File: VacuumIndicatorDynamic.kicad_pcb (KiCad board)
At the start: 2 copper layers, 151.2 x 100 mm, 113 parts, among them J1 Conn_01x02_Male, J2 Conn_01x03_Male, J3 Conn_01x03_Male, J4 Conn_01x03_Male, SW1 SW_DIP_x01, SW2 SW_DIP_x01, SW3 SW_DIP_x01, SW4 SW_DIP_x01, U1 AP1117-25, U2 YAAJ_BluePill

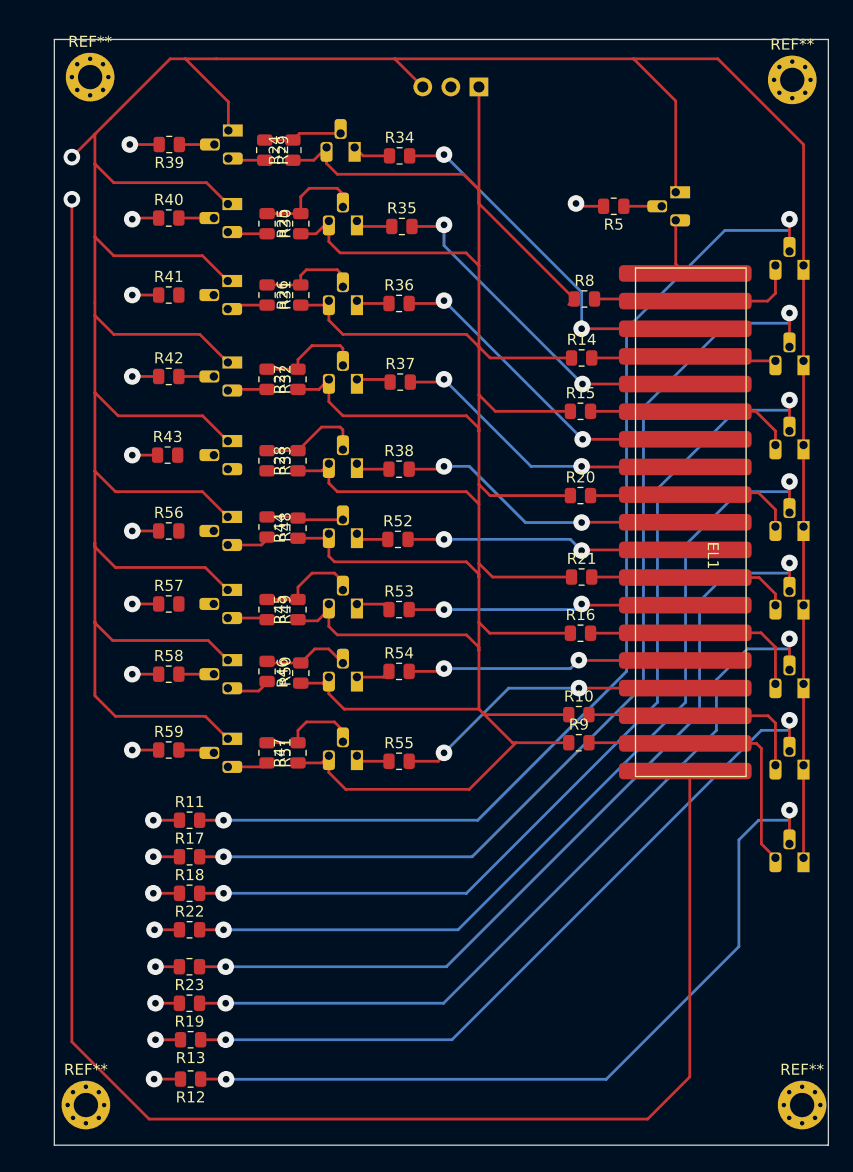
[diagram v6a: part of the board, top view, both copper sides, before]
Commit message: pcb route width update. add small copper area
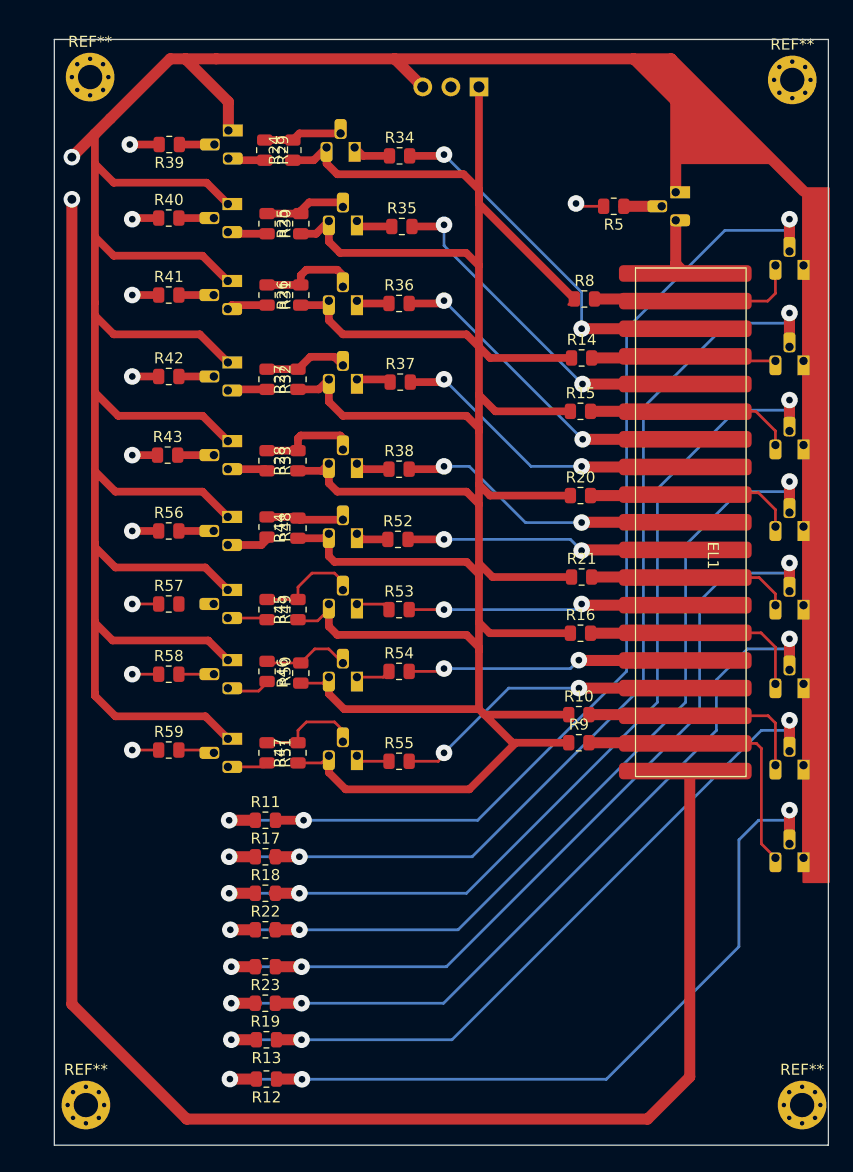
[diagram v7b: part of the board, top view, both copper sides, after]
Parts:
- moved R11 6.86 mm to (126.1, 94.0)
- moved R12 6.86 mm to (126.2, 117.4)
- moved R13 6.86 mm to (126.2, 113.8)
- moved R17 6.86 mm to (126.1, 97.3)
- moved R18 6.86 mm to (126.1, 100.6)
- moved R19 6.86 mm to (126.1, 110.5)
- moved R22 6.86 mm to (126.1, 103.9)
- moved R23 6.86 mm to (126.1, 107.2)
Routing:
- net Net-(R33-Pad2): track 0.00 -> 3.61 mm
- net Net-(R43-Pad2): track 0.00 -> 3.27 mm
- net Net-(R56-Pad2): track 0.00 -> 3.15 mm
- net Net-(R41-Pad2): track 0.00 -> 3.15 mm
- net Net-(R25-Pad2): track 10.5 -> 7.98 mm
- net GND: track 591.5 -> 589.0 mm
- net Net-(R27-Pad2): track 9.89 -> 7.64 mm
- net +2V5: track 193.1 -> 191.1 mm
